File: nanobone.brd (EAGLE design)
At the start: 30.5 x 30.5 mm, 51 parts, among them J1 USD_CONNECTOR, U1 24LC_32AT-I/OT, U2 OSD3358, U3 SN74LVC1G07_DCK_5, Y1 CM200C-32.768KAZF-UT, Y2 445C33D24M00000

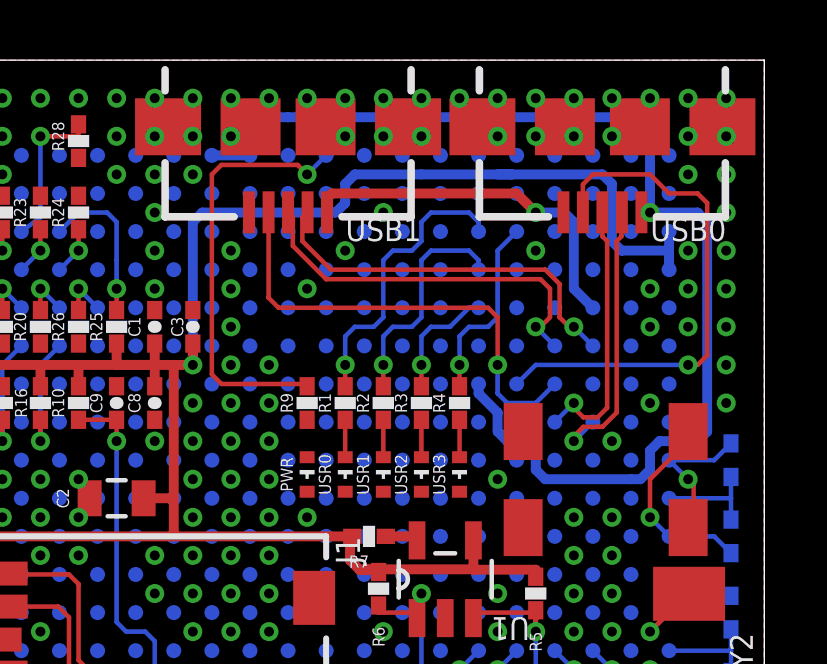
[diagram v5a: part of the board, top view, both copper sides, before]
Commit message: Fix USB_DC leftover trace. Define 6mil isolation for pour polygons.
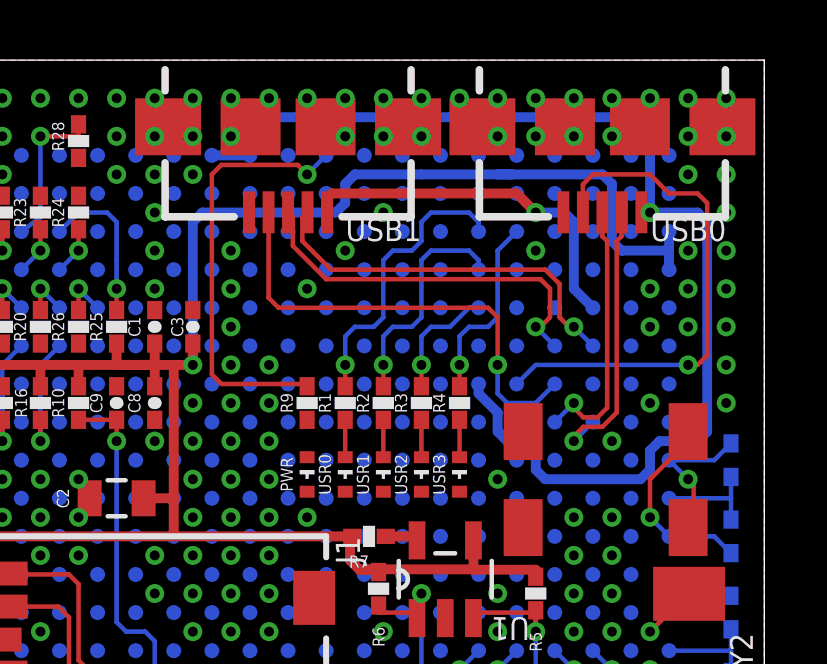
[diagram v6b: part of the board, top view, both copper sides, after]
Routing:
- net USB_DC: track 39.5 -> 38.9 mm
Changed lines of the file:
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@@
 <?xml version="1.0" encoding="utf-8"?>
 <!DOCTYPE eagle SYSTEM "eagle.dtd">
-<eagle version="7.5.0">
+<eagle version="7.6.0">
 <drawing>
 <settings>
@@
 <setting verticaltext="up"/>
 </settings>
-<grid distance="0.00625" unitdist="inch" unit="inch" style="lines" multiple="8" display="yes" altdistance="0.635" altunitdist="mm" altunit="mm"/>
+<grid distance="0.05" unitdist="inch" unit="inch" style="lines" multiple="8" display="yes" altdistance="0.005" altunitdist="inch" altunit="inch"/>
 <layers>
 <layer number="1" name="Top" color="4" fill="1" visible="yes" active="yes"/>
@@
 <layer number="19" name="Unrouted" color="6" fill="1" visible="yes" active="yes"/>
 <layer number="20" name="Dimension" color="15" fill="1" visible="yes" active="yes"/>
-<layer number="21" name="tPlace" color="7" fill="1" visible="yes" active="yes"/>
-<layer number="22" name="bPlace" color="7" fill="1" visible="yes" active="yes"/>
+<layer number="21" name="tPlace" color="16" fill="1" visible="yes" active="yes"/>
+<layer number="22" name="bPlace" color="14" fill="1" visible="yes" active="yes"/>
 <layer number="23" name="tOrigins" color="15" fill="1" visible="yes" active="yes"/>
 <layer number="24" name="bOrigins" color="15" fill="1" visible="yes" active="yes"/>
@@
 <layer number="27" name="tValues" color="7" fill="1" visible="yes" active="yes"/>
 <layer number="28" name="bValues" color="7" fill="1" visible="yes" active="yes"/>
-<layer number="29" name="tStop" color="7" fill="3" visible="no" active="yes"/>
-<layer number="30" name="bStop" color="7" fill="6" visible="no" active="yes"/>
+<layer number="29" name="tStop" color="7" fill="3" visible="yes" active="yes"/>
+<layer number="30" name="bStop" color="7" fill="6" visible="yes" active="yes"/>
 <layer number="31" name="tCream" color="7" fill="4" visible="no" active="yes"/>
 <layer number="32" name="bCream" color="7" fill="5" visible="no" active="yes"/>
@@
 <layer number="37" name="tTest" color="7" fill="1" visible="no" active="yes"/>
 <layer number="38" name="bTest" color="7" fill="1" visible="no" active="yes"/>
-<layer number="39" name="tKeepout" color="4" fill="11" visible="yes" active="yes"/>
-<layer number="40" name="bKeepout" color="1" fill="11" visible="yes" active="yes"/>
-<layer number="41" name="tRestrict" color="4" fill="10" visible="yes" active="yes"/>
-<layer number="42" name="bRestrict" color="1" fill="10" visible="yes" active="yes"/>
-<layer number="43" name="vRestrict" color="2" fill="10" visible="yes" active="yes"/>
+<layer number="39" name="tKeepout" color="4" fill="11" visible="no" active="yes"/>
+<layer number="40" name="bKeepout" color="1" fill="11" visible="no" active="yes"/>
+<layer number="41" name="tRestrict" color="4" fill="10" visible="no" active="yes"/>
+<layer number="42" name="bRestrict" color="1" fill="10" visible="no" active="yes"/>
+<layer number="43" name="vRestrict" color="2" fill="10" visible="no" active="yes"/>
 <layer number="44" name="Drills" color="7" fill="1" visible="no" active="yes"/>
 <layer number="45" name="Holes" color="7" fill="1" visible="yes" active="yes"/>
-<layer number="46" name="Milling" color="3" fill="1" visible="no" active="yes"/>
+<layer number="46" name="Milling" color="3" fill="1" visible="yes" active="yes"/>
 <layer number="47" name="Measures" color="7" fill="1" visible="no" active="yes"/>
 <layer number="48" name="Document" color="7" fill="1" visible="yes" active="yes"/>
 <layer number="49" name="Reference" color="7" fill="1" visible="yes" active="yes"/>
 <layer number="50" name="dxf" color="7" fill="1" visible="no" active="no"/>
-<layer number="51" name="tDocu" color="7" fill="1" visible="yes" active="yes"/>
+<layer number="51" name="tDocu" color="6" fill="1" visible="yes" active="yes"/>
 <layer number="52" name="bDocu" color="7" fill="1" visible="yes" active="yes"/>
 <layer number="53" name="tGND_GNDA" color="7" fill="9" visible="no" active="no"/>
@@
 <contactref element="USB0" pad="VBUS"/>
 <via x="26.67" y="25.4" extent="1-16" drill="0.3302" shape="octagon"/>
-<wire x1="14.605" y1="28.575" x2="20.32" y2="28.575" width="0.3302" layer="16"/>
-<wire x1="20.32" y1="28.575" x2="26.3525" y2="28.575" width="0.3302" layer="16"/>
 <wire x1="26.3525" y1="28.575" x2="26.67" y2="28.2575" width="0.3302" layer="16"/>
 <wire x1="26.67" y1="28.2575" x2="26.67" y2="25.4" width="0.3302" layer="16"/>
 <wire x1="13.335" y1="27.305" x2="13.335" y2="28.2575" width="0.3302" layer="16"/>
 <wire x1="13.335" y1="28.2575" x2="13.6525" y2="28.575" width="0.3302" layer="16"/>
-<wire x1="13.6525" y1="28.575" x2="14.605" y2="28.575" width="0.3302" layer="16"/>
-<wire x1="20.32" y1="27.94" x2="20.32" y2="28.575" width="0.3302" layer="16"/>
 <wire x1="26.67" y1="25.4" x2="26.3825" y2="25.4075" width="0.3302" layer="1"/>
 <wire x1="21.9075" y1="17.78" x2="22.5425" y2="17.78" width="0.3302" layer="16"/>
@@
 <wire x1="22.86" y1="17.4625" x2="22.86" y2="16.8275" width="0.3302" layer="16"/>
 <wire x1="22.86" y1="16.8275" x2="23.1775" y2="16.51" width="0.3302" layer="16"/>
-<wire x1="23.1775" y1="16.51" x2="26.035" y2="16.51" width="0.3302" layer="16"/>
-<wire x1="26.035" y1="16.51" x2="26.3525" y2="16.51" width="0.3302" layer="16"/>
+<wire x1="23.1775" y1="16.51" x2="26.3525" y2="16.51" width="0.3302" layer="16"/>
 <wire x1="26.3525" y1="16.51" x2="26.67" y2="16.8275" width="0.3302" layer="16"/>
 <wire x1="26.67" y1="16.8275" x2="26.67" y2="17.4625" width="0.3302" layer="16"/>
@@
 <wire x1="20.955" y1="19.3675" x2="21.59" y2="18.7325" width="0.3302" layer="16"/>
 <wire x1="21.59" y1="18.7325" x2="21.59" y2="18.0975" width="0.3302" layer="16"/>
+<wire x1="26.3525" y1="28.575" x2="13.6525" y2="28.575" width="0.3302" layer="16"/>
 </signal>
 <signal name="N$12">
@@
 <contactref element="RESET" pad="1"/>
 <contactref element="POWER" pad="1"/>
-<polygon width="0.3302" layer="1">
+<polygon width="0.3302" layer="1" isolate="0.1524">
 <vertex x="30.48" y="30.48"/>
 <vertex x="0" y="30.48"/>
@@
 <vertex x="30.48" y="0"/>
 </polygon>
-<polygon width="0.3302" layer="16">
+<polygon width="0.3302" layer="16" isolate="0.1524">
 <vertex x="30.48" y="30.48"/>
 <vertex x="0" y="30.48"/>
